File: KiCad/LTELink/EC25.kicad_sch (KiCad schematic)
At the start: 23 parts, among them J4 1759547-1, Q2 AO3401A, SW2 SW_SPDT, U1 LM29300T-3.3

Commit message: Progress on V2.0 and file structure reformat
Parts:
- removed LED2: KT-0805G, LED_SMD:LED_0805_2012Metric, symbol LTELink:GREEN LED
- removed LED6: KT-0603W, LED_SMD:LED_0603_1608Metric, symbol LTELink:WHITE LED
- added D10: LED, LED_SMD:LED_0603_1608Metric, symbol Device:LED
- added D9: LED, LED_SMD:LED_0805_2012Metric, symbol Device:LED
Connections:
- net GND: now also D9.1 (K); no longer J4.53 (NUT), J4.S1
- net at J4.42 (~{LED_WWAN}): now also D10.1 (K)
- net at R5.1: now also D9.2 (A)
- net at R16.1: now also D10.2 (A)
- no-connect marks 14 -> 16

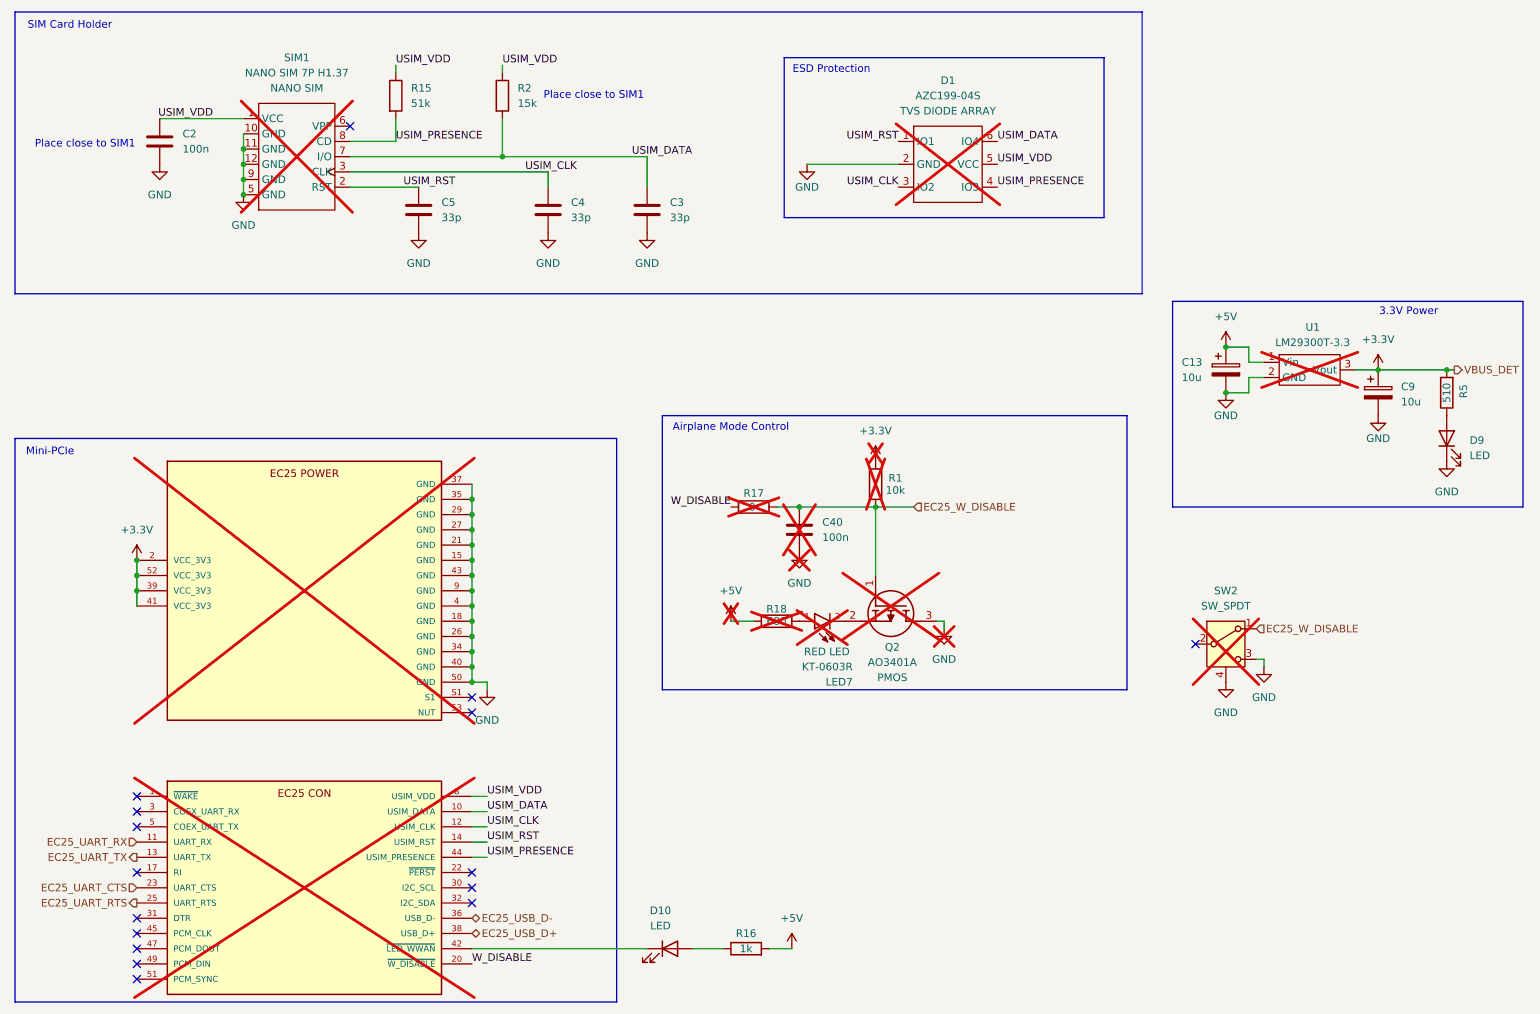
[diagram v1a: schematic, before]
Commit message: Moved LEDs to other side of the board, which means they mustbe assembled by hand. Added UART 5 test points.
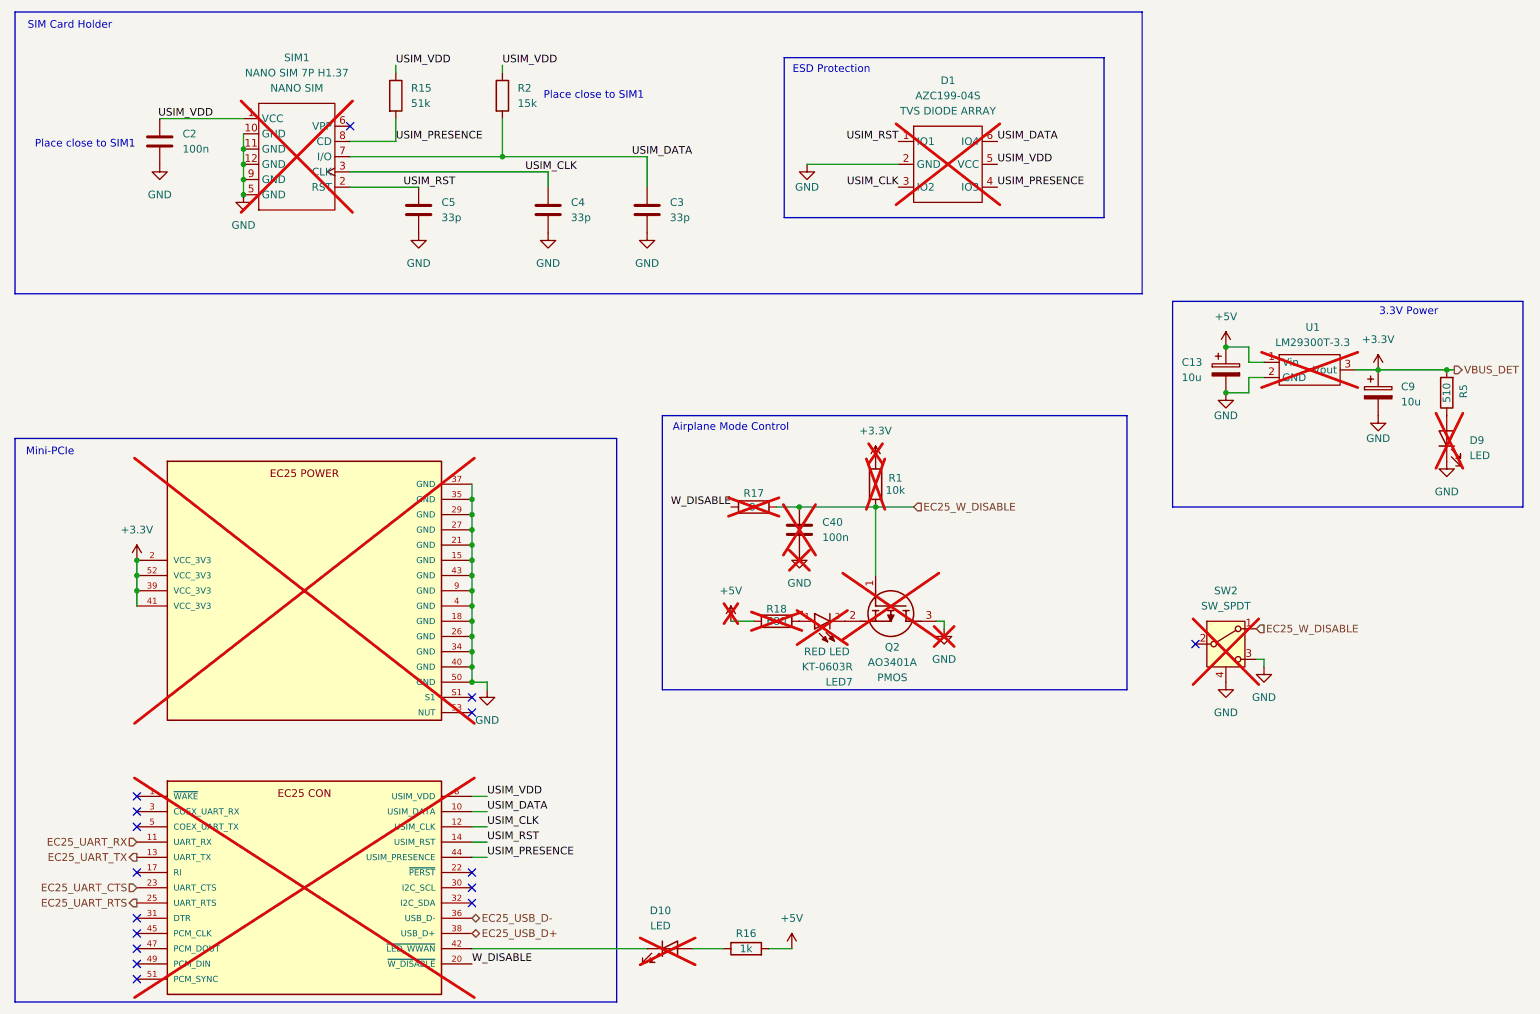
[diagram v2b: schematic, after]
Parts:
- D10: footprint LED_SMD:LED_0603_1608Metric -> LED_SMD:LED_0805_2012Metric_Pad1.15x1.40mm_HandSolder; now not fitted
- D9: footprint LED_SMD:LED_0805_2012Metric -> LED_SMD:LED_0805_2012Metric_Pad1.15x1.40mm_HandSolder; now not fitted
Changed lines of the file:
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@@
 		(on_board yes)
 		(in_pos_files yes)
-		(dnp no)
+		(dnp yes)
 		(fields_autoplaced yes)
 		(property "Reference" "D9"
@@
 			)
 		)
-		(property "Footprint" "LED_SMD:LED_0805_2012Metric"
+		(property "Footprint" "LED_SMD:LED_0805_2012Metric_Pad1.15x1.40mm_HandSolder"
 			(at 266.7 92.71 0)
 			(hide yes)
@@
 		(on_board yes)
 		(in_pos_files yes)
-		(dnp no)
+		(dnp yes)
 		(fields_autoplaced yes)
 		(property "Reference" "D10"
@@
 			)
 		)
-		(property "Footprint" "LED_SMD:LED_0603_1608Metric"
+		(property "Footprint" "LED_SMD:LED_0805_2012Metric_Pad1.15x1.40mm_HandSolder"
 			(at 137.16 177.8 0)
 			(hide yes)
